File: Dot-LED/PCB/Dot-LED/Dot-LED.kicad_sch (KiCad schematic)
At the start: 1 part

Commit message: Start inital dotLED KiCad design
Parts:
- N1: value (none) -> V20220506; footprint (none) -> SquantorLabels:Label_Generic
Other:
- added sheet Battery_Regulator (Battery_Regulator.kicad_sch)
- added sheet Buck_Boost (Buck_Boost.kicad_sch)
- added sheet ESP32C3_MCU (ESP32C3_MCU.kicad_sch)
- added sheet IOConnectors (IOConnectors.kicad_sch)

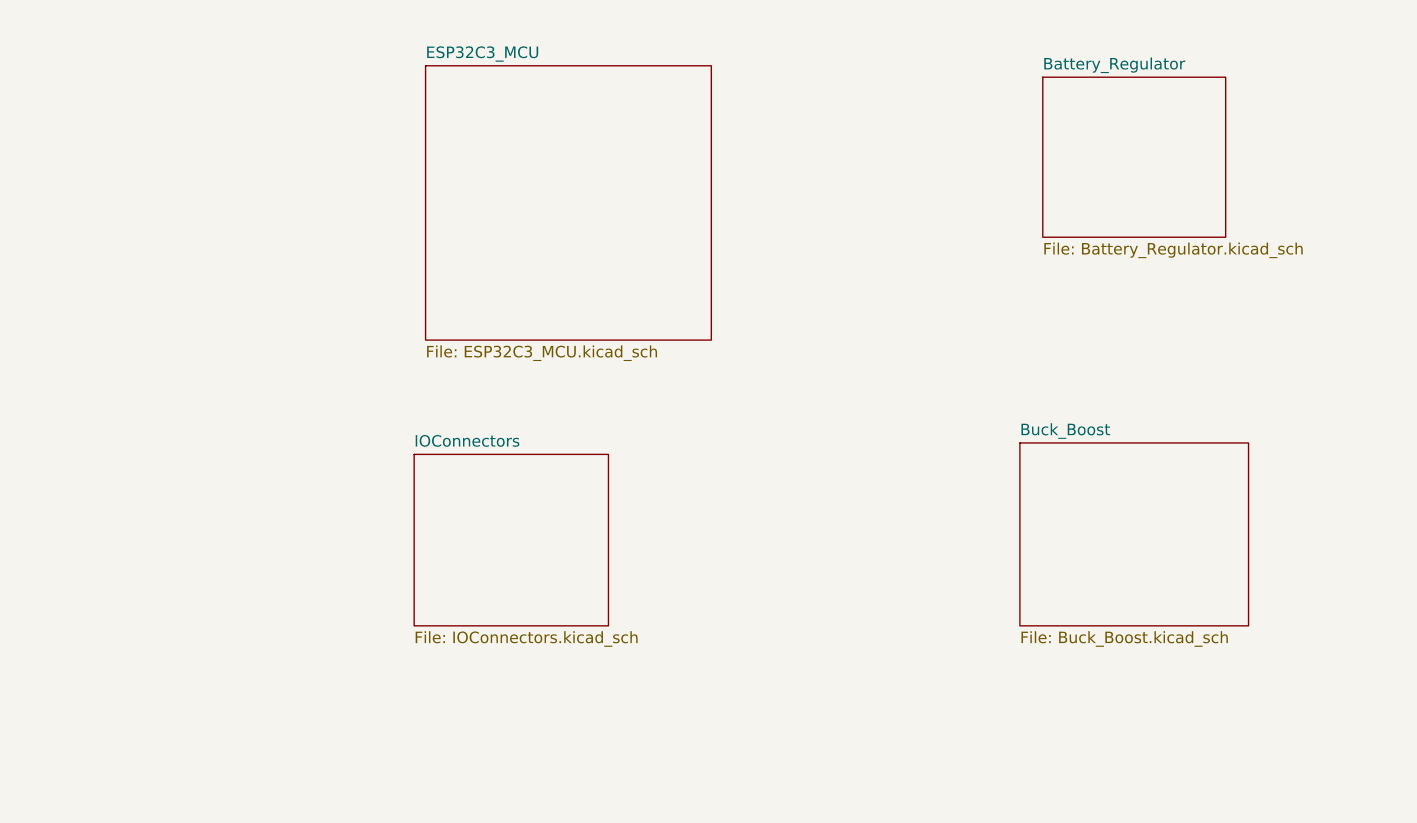
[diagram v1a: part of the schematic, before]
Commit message: add common KiCad library using plugin
https://componentsearchengine.com/ga/downloads.php
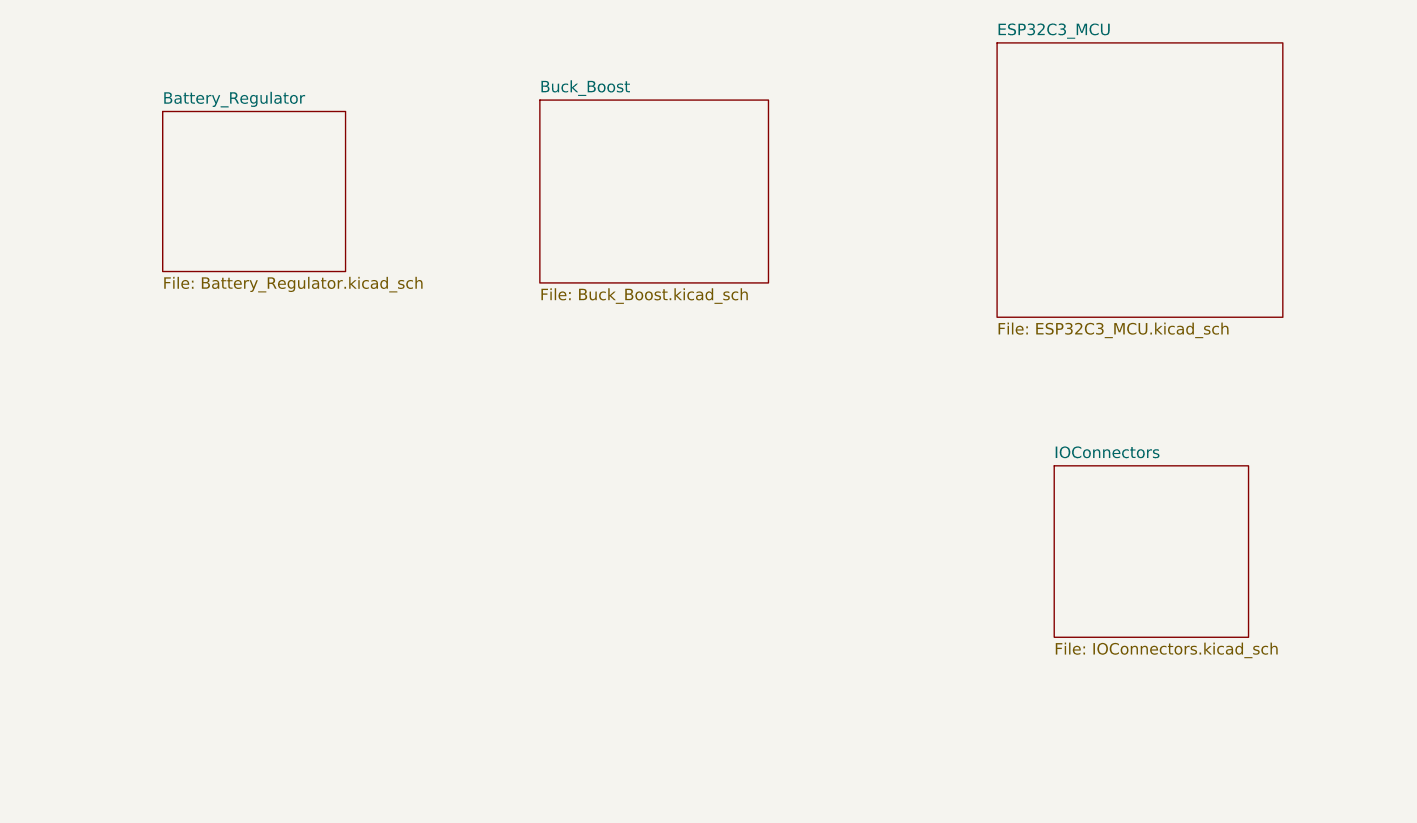
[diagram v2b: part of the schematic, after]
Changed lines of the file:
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@@
     )
   )
-  (sheet (at 77.47 73.66) (size 21.59 19.05) (fields_autoplaced)
+  (sheet (at 148.59 74.93) (size 21.59 19.05) (fields_autoplaced)
     (stroke (width 0.1524) (type solid))
     (fill (color 0 0 0 0.0000))
-    (property "Sheetname" "IOConnectors" (at 77.47 72.9484 0)
+    (property "Sheetname" "IOConnectors" (at 148.59 74.2184 0)
       (effects (font (size 1.27 1.27)) (justify left bottom))
     )
-    (property "Sheetfile" "IOConnectors.kicad_sch" (at 77.47 93.2946 0)
+    (property "Sheetfile" "IOConnectors.kicad_sch" (at 148.59 94.5646 0)
       (effects (font (size 1.27 1.27)) (justify left top))
     )
@@
     )
   )
-  (sheet (at 78.74 30.48) (size 31.75 30.48) (fields_autoplaced)
+  (sheet (at 142.24 27.94) (size 31.75 30.48) (fields_autoplaced)
     (stroke (width 0.1524) (type solid))
     (fill (color 0 0 0 0.0000))
-    (property "Sheetname" "ESP32C3_MCU" (at 78.74 29.7684 0)
+    (property "Sheetname" "ESP32C3_MCU" (at 142.24 27.2284 0)
       (effects (font (size 1.27 1.27)) (justify left bottom))
     )
-    (property "Sheetfile" "ESP32C3_MCU.kicad_sch" (at 78.74 61.5446 0)
+    (property "Sheetfile" "ESP32C3_MCU.kicad_sch" (at 142.24 59.0046 0)
       (effects (font (size 1.27 1.27)) (justify left top))
     )
@@
     )
   )
-  (sheet (at 147.32 31.75) (size 20.32 17.78) (fields_autoplaced)
+  (sheet (at 49.53 35.56) (size 20.32 17.78) (fields_autoplaced)
     (stroke (width 0.1524) (type solid))
     (fill (color 0 0 0 0.0000))
-    (property "Sheetname" "Battery_Regulator" (at 147.32 31.0384 0)
+    (property "Sheetname" "Battery_Regulator" (at 49.53 34.8484 0)
       (effects (font (size 1.27 1.27)) (justify left bottom))
     )
-    (property "Sheetfile" "Battery_Regulator.kicad_sch" (at 147.32 50.1146 0)
+    (property "Sheetfile" "Battery_Regulator.kicad_sch" (at 49.53 53.9246 0)
       (effects (font (size 1.27 1.27)) (justify left top))
     )
@@
     )
   )
-  (sheet (at 144.78 72.39) (size 25.4 20.32) (fields_autoplaced)
+  (sheet (at 91.44 34.29) (size 25.4 20.32) (fields_autoplaced)
     (stroke (width 0.1524) (type solid))
     (fill (color 0 0 0 0.0000))
-    (property "Sheetname" "Buck_Boost" (at 144.78 71.6784 0)
+    (property "Sheetname" "Buck_Boost" (at 91.44 33.5784 0)
       (effects (font (size 1.27 1.27)) (justify left bottom))
     )
-    (property "Sheetfile" "Buck_Boost.kicad_sch" (at 144.78 93.2946 0)
+    (property "Sheetfile" "Buck_Boost.kicad_sch" (at 91.44 55.1946 0)
       (effects (font (size 1.27 1.27)) (justify left top))
     )

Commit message: Update DotLED Schem
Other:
- sheet Battery_Regulator ports: added VBAT, VDD_IN; removed none
- sheet Buck_Boost ports: added 3V3_VCC, V_Bat, V_USB; removed none
- sheet ESP32C3_MCU ports: added 3V3_VCC, D1, D2, D3, D4, D5, D8, D9, ESP_DN, ESP_DP, RX_D7, TX_D6; removed none
- sheet IOConnectors ports: added 3V3, D1, D2, D3, D4, D6, D7, D8, D9, LED_Data, USB_D+, USB_D-, V_USB; removed none

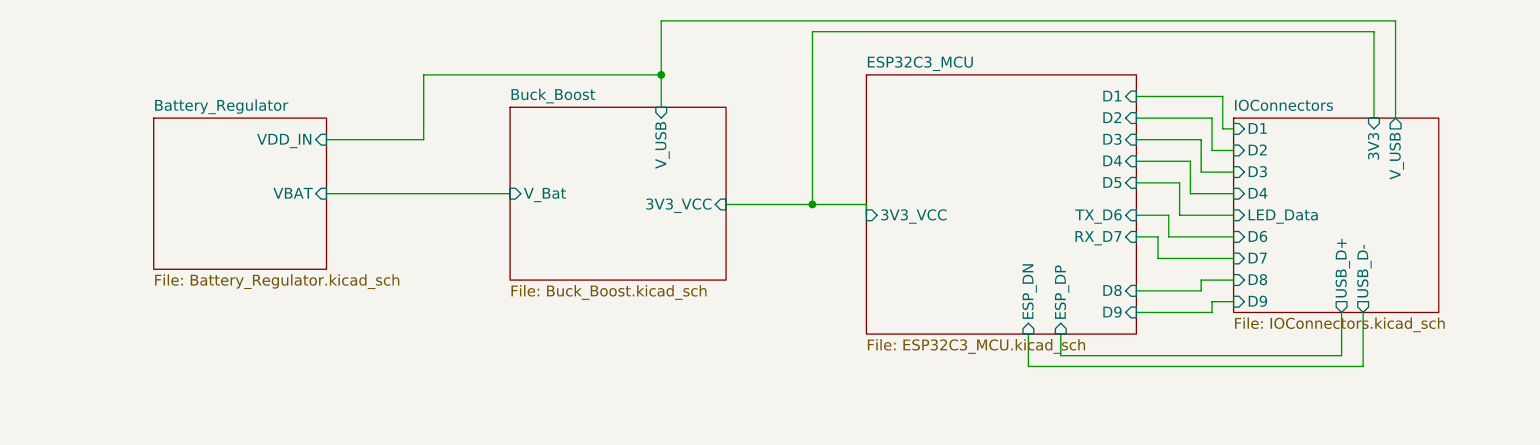
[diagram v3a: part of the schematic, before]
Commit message: update DotLED
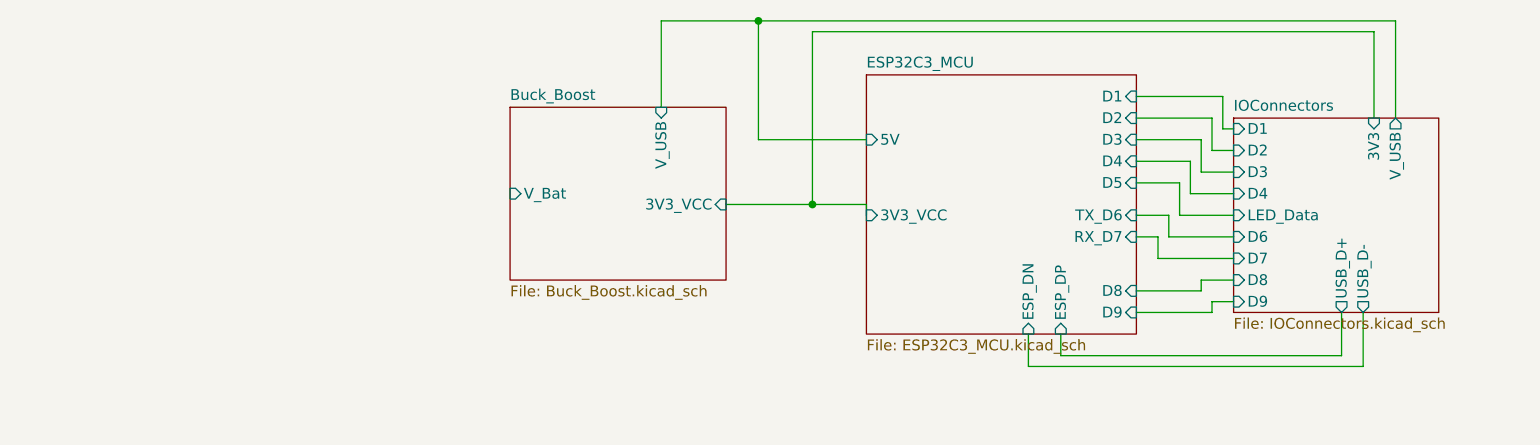
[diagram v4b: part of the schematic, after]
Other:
- removed sheet Battery_Regulator
- sheet ESP32C3_MCU ports: added 5V; removed none
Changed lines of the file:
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@@
   (junction (at 127 45.72) (diameter 0) (color 0 0 0 0)
   )
-  (junction (at 109.22 30.48) (diameter 0) (color 0 0 0 0)
+  (junction (at 120.65 24.13) (diameter 0) (color 0 0 0 0)
   )
   (wire (pts (xy 173.99 58.42) (xy 173.99 57.15))
@@
     (stroke (width 0) (type default))
   )
-  (wire (pts (xy 109.22 24.13) (xy 109.22 30.48))
-    (stroke (width 0) (type default))
-  )
   (wire (pts (xy 171.45 44.45) (xy 176.53 44.45))
     (stroke (width 0) (type default))
@@
     (stroke (width 0) (type default))
   )
-  (wire (pts (xy 109.22 34.29) (xy 109.22 30.48))
+  (wire (pts (xy 109.22 24.13) (xy 109.22 34.29))
     (stroke (width 0) (type default))
   )
@@
     (stroke (width 0) (type default))
   )
-  (wire (pts (xy 195.58 24.13) (xy 109.22 24.13))
+  (wire (pts (xy 195.58 24.13) (xy 120.65 24.13))
     (stroke (width 0) (type default))
   )
@@
     (stroke (width 0) (type default))
   )
+  (wire (pts (xy 133.35 38.1) (xy 120.65 38.1))
+    (stroke (width 0) (type default))
+  )
   (polyline (pts (xy 162.56 180.34) (xy 162.56 184.15))
     (stroke (width 0) (type default))
@@
     (stroke (width 0) (type default))
   )
-  (wire (pts (xy 81.28 30.48) (xy 81.28 38.1))
-    (stroke (width 0) (type default))
-  )
   (polyline (pts (xy 175.26 196.85) (xy 175.26 185.42))
     (stroke (width 0) (type default))
@@
     (stroke (width 0) (type default))
   )
+  (wire (pts (xy 120.65 24.13) (xy 109.22 24.13))
+    (stroke (width 0) (type default))
+  )
   (wire (pts (xy 173.99 39.37) (xy 176.53 39.37))
     (stroke (width 0) (type default))
@@
     (stroke (width 0) (type default))
   )
+  (wire (pts (xy 120.65 38.1) (xy 120.65 24.13))
+    (stroke (width 0) (type default))
+  )
   (wire (pts (xy 175.26 33.02) (xy 175.26 36.83))
     (stroke (width 0) (type default))
@@
     (stroke (width 0) (type default))
   )
-  (wire (pts (xy 69.85 44.45) (xy 91.44 44.45))
-    (stroke (width 0) (type default))
-  )
   (wire (pts (xy 172.72 55.88) (xy 172.72 54.61))
     (stroke (width 0) (type default))
   )
-  (wire (pts (xy 81.28 38.1) (xy 69.85 38.1))
-    (stroke (width 0) (type default))
-  )
   (polyline (pts (xy 17.78 191.77) (xy 17.78 195.58))
     (stroke (width 0) (type default))
@@
   )
   (wire (pts (xy 165.1 33.02) (xy 175.26 33.02))
-    (stroke (width 0) (type default))
-  )
-  (wire (pts (xy 109.22 30.48) (xy 81.28 30.48))
     (stroke (width 0) (type default))
   )
@@
       (effects (font (size 1.27 1.27)) (justify right))
     )
+    (pin "5V" input (at 133.35 38.1 180)
+      (effects (font (size 1.27 1.27)) (justify left))
+    )
     (instances
       (project "Dot-LED"
@@
       )
     )
-  )
-  (sheet (at 49.53 35.56) (size 20.32 17.78) (fields_autoplaced)
-    (stroke (width 0.1524) (type solid))
-    (fill (color 0 0 0 0.0000))
-    (property "Sheetname" "Battery_Regulator" (at 49.53 34.8484 0)
-      (effects (font (size 1.27 1.27)) (justify left bottom))
-    )
-    (property "Sheetfile" "Battery_Regulator.kicad_sch" (at 49.53 53.9246 0)
-      (effects (font (size 1.27 1.27)) (justify left top))
-    )
-    (pin "VDD_IN" input (at 69.85 38.1 0)
-      (effects (font (size 1.27 1.27)) (justify right))
-    )
-    (pin "VBAT" input (at 69.85 44.45 0)
-      (effects (font (size 1.27 1.27)) (justify right))
-    )
-    (instances
-      (project "Dot-LED"
-        (path "/e63e39d7-6ac0-4ffd-8aa3-1841a4541b55" (page "3"))
-      )
-    )

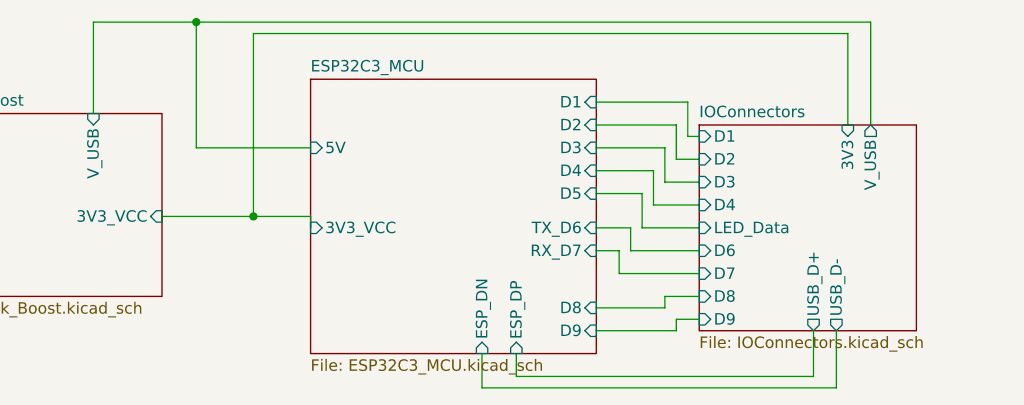
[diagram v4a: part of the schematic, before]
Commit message: Init layout for DotLED
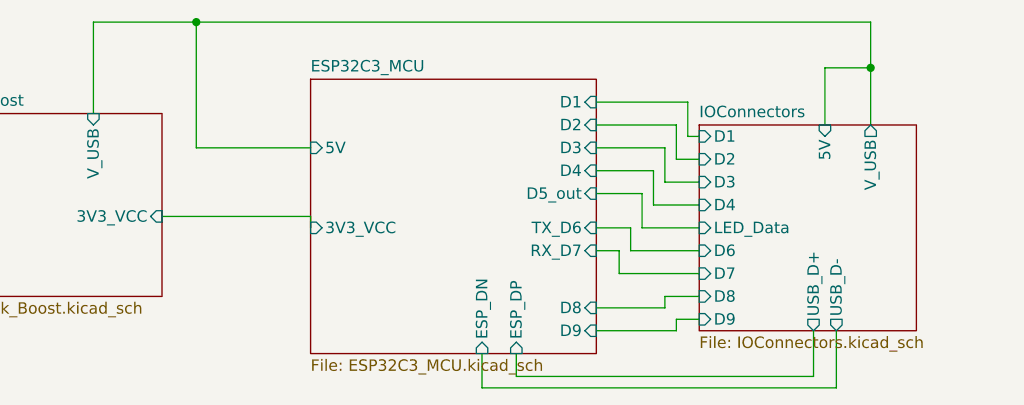
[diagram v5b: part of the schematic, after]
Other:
- sheet ESP32C3_MCU ports: added D5_out; removed D5
- sheet IOConnectors ports: added 5V; removed 3V3
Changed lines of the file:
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@@
 (kicad_sch (version 20230121) (generator eeschema)
   (paper "A4")
-  (junction (at 127 45.72) (diameter 0) (color 0 0 0 0)
+  (junction (at 195.58 29.21) (diameter 0) (color 0 0 0 0)
   )
   (junction (at 120.65 24.13) (diameter 0) (color 0 0 0 0)
@@
     (stroke (width 0) (type default))
   )
+  (wire (pts (xy 195.58 29.21) (xy 195.58 24.13))
+    (stroke (width 0) (type default))
+  )
   (wire (pts (xy 171.45 44.45) (xy 176.53 44.45))
     (stroke (width 0) (type default))
@@
     (stroke (width 0) (type default))
   )
-  (wire (pts (xy 193.04 25.4) (xy 193.04 35.56))
-    (stroke (width 0) (type default))
-  )
   (wire (pts (xy 168.91 49.53) (xy 176.53 49.53))
     (stroke (width 0) (type default))
@@
     (stroke (width 0) (type default))
   )
-  (wire (pts (xy 195.58 35.56) (xy 195.58 24.13))
+  (wire (pts (xy 195.58 35.56) (xy 195.58 29.21))
     (stroke (width 0) (type default))
   )
@@
     (stroke (width 0) (type default))
   )
-  (wire (pts (xy 116.84 45.72) (xy 127 45.72))
-    (stroke (width 0) (type default))
-  )
   (wire (pts (xy 195.58 24.13) (xy 120.65 24.13))
     (stroke (width 0) (type default))
@@
     (stroke (width 0) (type default))
   )
+  (wire (pts (xy 190.5 35.56) (xy 190.5 29.21))
+    (stroke (width 0) (type default))
+  )
   (wire (pts (xy 133.35 38.1) (xy 120.65 38.1))
     (stroke (width 0) (type default))
@@
     (stroke (width 0) (type default))
   )
-  (wire (pts (xy 127 25.4) (xy 193.04 25.4))
-    (stroke (width 0) (type default))
-  )
   (wire (pts (xy 120.65 24.13) (xy 109.22 24.13))
     (stroke (width 0) (type default))
@@
     (stroke (width 0) (type default))
   )
-  (wire (pts (xy 127 45.72) (xy 127 25.4))
-    (stroke (width 0) (type default))
-  )
   (wire (pts (xy 170.18 46.99) (xy 170.18 43.18))
     (stroke (width 0) (type default))
@@
     (stroke (width 0) (type default))
   )
+  (wire (pts (xy 190.5 29.21) (xy 195.58 29.21))
+    (stroke (width 0) (type default))
+  )
   (wire (pts (xy 120.65 38.1) (xy 120.65 24.13))
     (stroke (width 0) (type default))
@@
     (stroke (width 0) (type default))
   )
-  (wire (pts (xy 127 45.72) (xy 133.35 45.72))
+  (wire (pts (xy 116.84 45.72) (xy 133.35 45.72))
     (stroke (width 0) (type default))
   )
@@
       (effects (font (size 1.27 1.27)) (justify left top))
     )
-    (pin "3V3" input (at 193.04 35.56 90)
-      (effects (font (size 1.27 1.27)) (justify right))
-    )
     (pin "LED_Data" input (at 176.53 46.99 180)
       (effects (font (size 1.27 1.27)) (justify left))
@@
     (pin "D4" input (at 176.53 44.45 180)
       (effects (font (size 1.27 1.27)) (justify left))
+    )
+    (pin "5V" input (at 190.5 35.56 90)
+      (effects (font (size 1.27 1.27)) (justify right))
     )
     (instances
@@
       (effects (font (size 1.27 1.27)) (justify left))
     )
-    (pin "D5" input (at 165.1 43.18 0)
-      (effects (font (size 1.27 1.27)) (justify right))
-    )
     (pin "D8" input (at 165.1 55.88 0)
       (effects (font (size 1.27 1.27)) (justify right))
@@
       (effects (font (size 1.27 1.27)) (justify left))
     )
-    (instances
+    (pin "D5_out" input (at 165.1 43.18 0)
+      (effects (font (size 1.27 1.27)) (justify right))
+    )
+    (instances
